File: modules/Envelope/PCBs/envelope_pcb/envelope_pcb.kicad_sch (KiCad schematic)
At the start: 6 parts, among them J10 Conn_01x08_Socket, J11 Conn_01x07_Pin, J12 Conn_01x07_Socket, J13 Eurorack_2x8_Power, J9 Conn_01x08_Pin

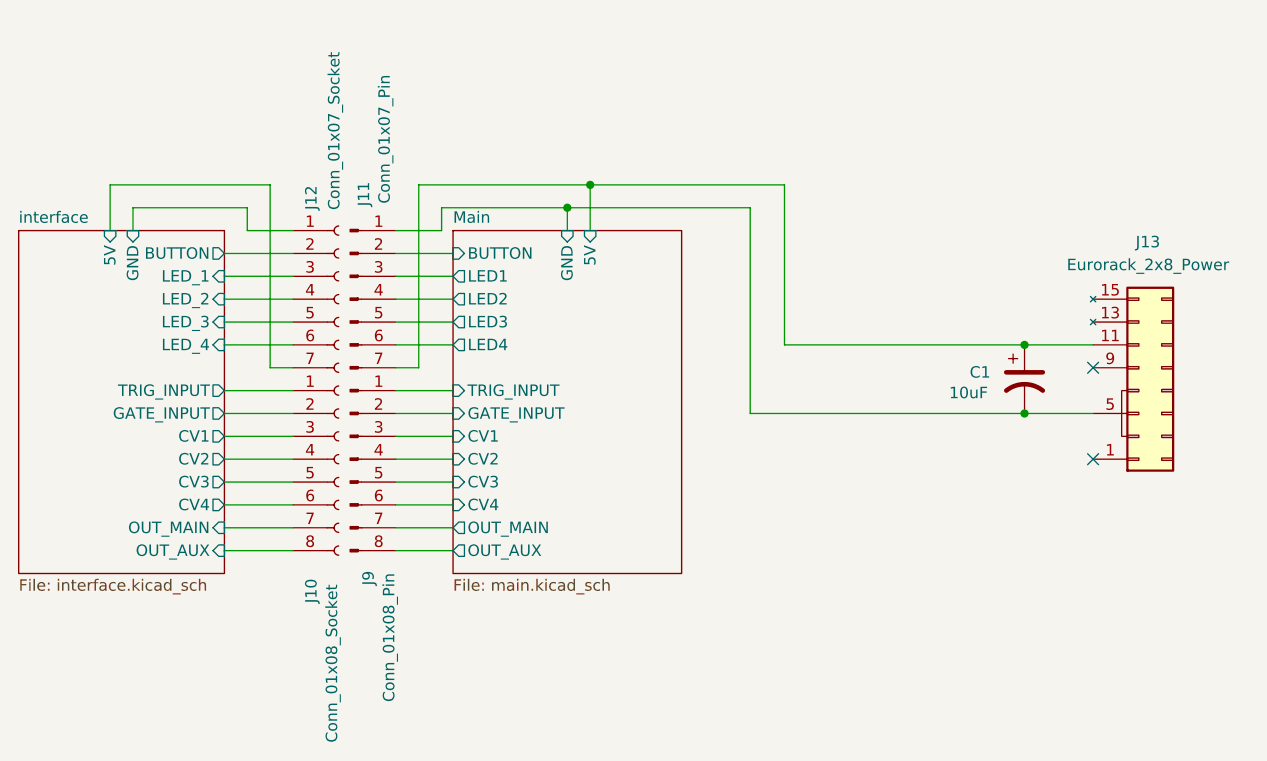
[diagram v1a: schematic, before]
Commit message: fix gate inputs for envelope
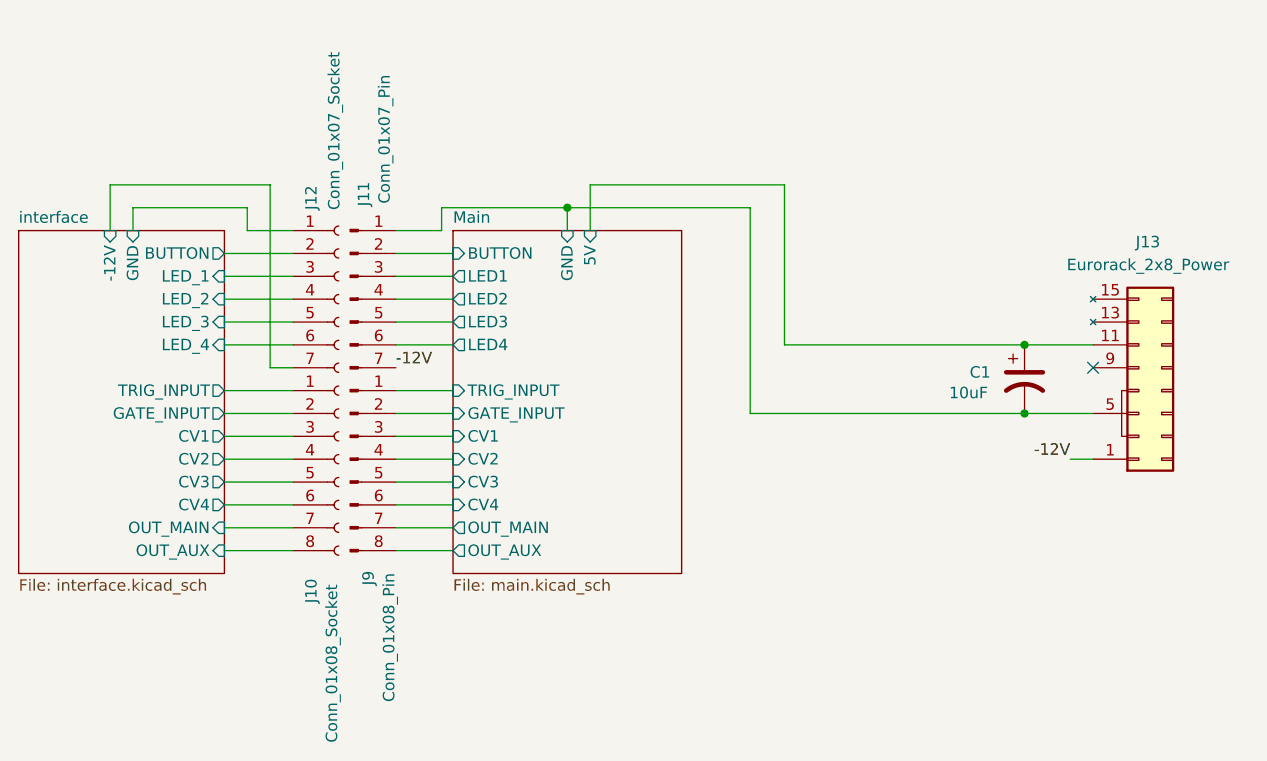
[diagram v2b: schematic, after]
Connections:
- net Main/5V: no longer J11.7 (Pin_7)
- net -12V: now reaches J13.1 (-12v), J13.2 (-12v)
- net -12V: now also J11.7 (Pin_7)
- net interface/5V renamed interface/-12V
- no-connect marks 2 -> 1
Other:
- sheet interface ports: added -12V; removed 5V
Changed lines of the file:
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@@
-	)
-	(junction
-		(at 114.3 45.72)
-		(diameter 0)
-		(color 0 0 0 0)
 	)
 	(junction
@@
 		(at 170.18 66.04)
 	)
-	(no_connect
-		(at 170.18 76.2)
-	)
 	(wire
 		(pts
@@
 	(wire
 		(pts
-			(xy 95.25 45.72) (xy 114.3 45.72)
-		)
-		(stroke
-			(width 0)
-			(type default)
-		)
-	)
-	(wire
-		(pts
 			(xy 114.3 45.72) (xy 135.89 45.72)
 		)
@@
 	(wire
 		(pts
-			(xy 95.25 45.72) (xy 95.25 66.04)
-		)
-		(stroke
-			(width 0)
-			(type default)
-		)
-	)
-	(wire
-		(pts
 			(xy 92.71 83.82) (xy 99.06 83.82)
 		)
@@
 	(wire
 		(pts
-			(xy 95.25 66.04) (xy 92.71 66.04)
-		)
-		(stroke
-			(width 0)
-			(type default)
-		)
-	)
-	(wire
-		(pts
 			(xy 78.74 45.72) (xy 78.74 66.04)
 		)
@@
 	(wire
 		(pts
+			(xy 167.64 76.2) (xy 170.18 76.2)
+		)
+		(stroke
+			(width 0)
+			(type default)
+		)
+	)
+	(wire
+		(pts
 			(xy 60.96 45.72) (xy 78.74 45.72)
 		)
@@
 			(width 0)
 			(type default)
+		)
+	)
+	(label "-12V"
+		(at 167.64 76.2 180)
+		(fields_autoplaced yes)
+		(effects
+			(font
+				(size 1.27 1.27)
+			)
+			(justify right bottom)
+		)
+	)
+	(label "-12V"
+		(at 92.71 66.04 0)
+		(fields_autoplaced yes)
+		(effects
+			(font
+				(size 1.27 1.27)
+			)
+			(justify left bottom)
 		)
 	)
@@
 			)
 		)
-		(pin "5V" input
+		(pin "-12V" input
 			(at 60.96 50.8 90)
 			(effects
